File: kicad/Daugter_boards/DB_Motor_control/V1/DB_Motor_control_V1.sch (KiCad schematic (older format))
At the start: 11 parts, among them P1 CONN_01X19, P2 CONN_01X05, P3 CONN_01X03, P4 CONN_01X19, Q1 Q2N2222

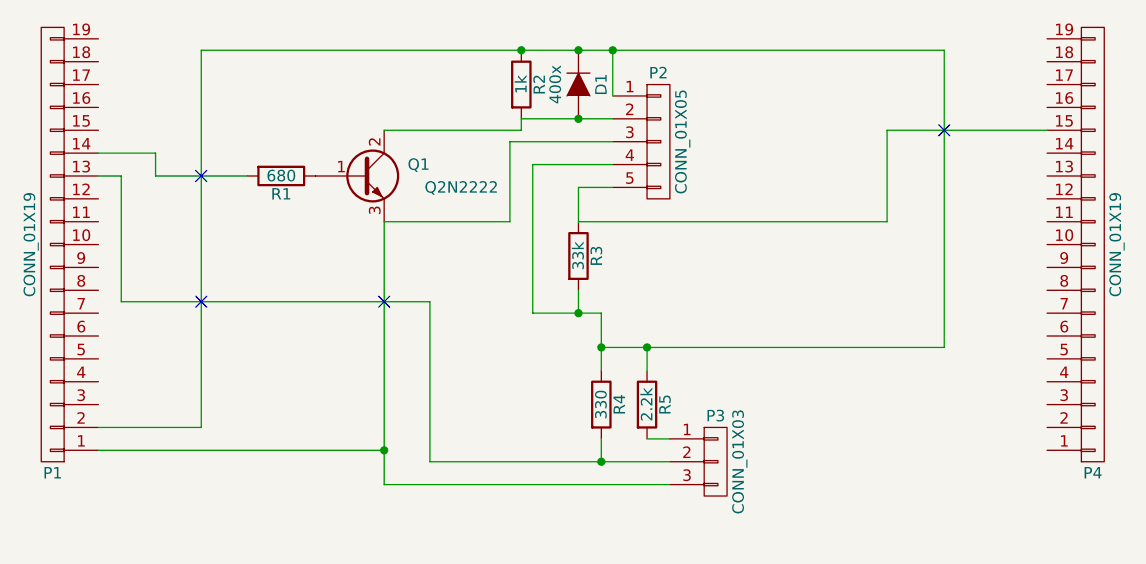
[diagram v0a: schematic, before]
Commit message: adding DB_Motor_Control
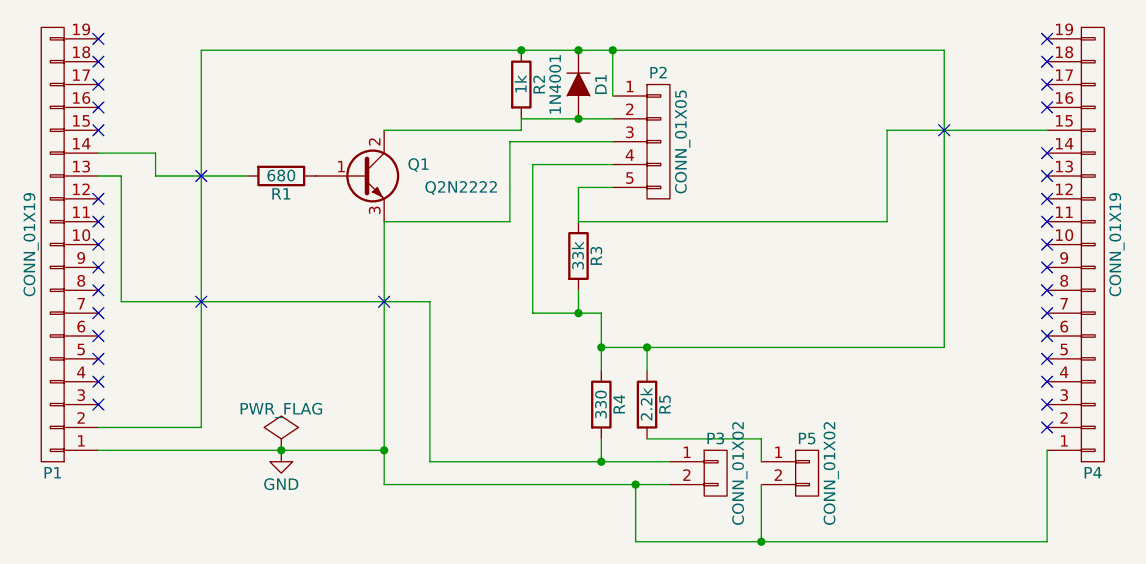
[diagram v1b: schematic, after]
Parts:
- removed P3: CONN_01X03, symbol CONN_01X03
- added P3, P5: CONN_01X02, Socket_Strips:Socket_Strip_Straight_1x02, symbol CONN_01X02
- D1: value 400x -> 1N4001; footprint (none) -> Diodes_ThroughHole:Diode_DO-35_SOD27_Horizontal_RM10
- P1, P4: footprint (none) -> Socket_Strips:Socket_Strip_Straight_1x19
- P2: footprint (none) -> Socket_Strips:Socket_Strip_Straight_1x05
- Q1: footprint (none) -> TO_SOT_Packages_THT:TO-18_3Pin
- R1, R2, R3, R4, R5: footprint (none) -> Resistors_ThroughHole:Resistor_Horizontal_RM10mm
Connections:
- net GND: now reaches P1.1 (P1), P2.3 (P3), Q1.3 (E)
- net GND: now also P4.1 (P1), P3.2 (P2), P5.2 (P2)
- net at R5.2: now also P5.1 (P1)
- net at P1.13 (P13), R4.2: now also P3.1 (P1)
- no-connect marks 4 -> 36
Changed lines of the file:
@@
 LIBS:valves
 LIBS:echopen
+LIBS:DB_Motor_control_V1-cache
 EELAYER 25 0
 EELAYER END
@@
 F 0 "R2" V 5280 2150 50  0000 C CNN
 F 1 "1k" V 5200 2150 50  0000 C CNN
-F 2 "" V 5130 2150 50  0000 C CNN
+F 2 "Resistors_ThroughHole:Resistor_Horizontal_RM10mm" V 5130 2150 50  0001 C CNN
 F 3 "" H 5200 2150 50  0000 C CNN
 	1    5200 2150
@@
 P 5450 2150
 F 0 "D1" H 5450 2250 50  0000 C CNN
-F 1 "400x" H 5450 2050 50  0000 C CNN
-F 2 "" H 5450 2150 50  0000 C CNN
+F 1 "1N4001" H 5450 2050 50  0000 C CNN
+F 2 "Diodes_ThroughHole:Diode_DO-35_SOD27_Horizontal_RM10" H 5450 2150 50  0001 C CNN
 F 3 "" H 5450 2150 50  0000 C CNN
 	1    5450 2150
@@
 F 0 "Q1" H 4800 2600 50  0000 R CNN
 F 1 "Q2N2222" H 5100 2500 50  0000 R CNN
-F 2 "" H 4700 2650 50  0000 C CNN
+F 2 "TO_SOT_Packages_THT:TO-18_3Pin" H 4700 2650 50  0001 C CNN
 F 3 "" H 4500 2550 50  0000 C CNN
 	1    4500 2550
@@
 F 0 "R1" V 4230 2550 50  0000 C CNN
 F 1 "680" V 4150 2550 50  0000 C CNN
-F 2 "" V 4080 2550 50  0000 C CNN
+F 2 "Resistors_ThroughHole:Resistor_Horizontal_RM10mm" V 4080 2550 50  0001 C CNN
 F 3 "" H 4150 2550 50  0000 C CNN
 	1    4150 2550
@@
 F 0 "R5" V 5830 3550 50  0000 C CNN
 F 1 "2.2k" V 5750 3550 50  0000 C CNN
-F 2 "" V 5680 3550 50  0000 C CNN
+F 2 "Resistors_ThroughHole:Resistor_Horizontal_RM10mm" V 5680 3550 50  0001 C CNN
 F 3 "" H 5750 3550 50  0000 C CNN
 	1    5750 3550
@@
 F 0 "R4" V 5630 3550 50  0000 C CNN
 F 1 "330" V 5550 3550 50  0000 C CNN
-F 2 "" V 5480 3550 50  0000 C CNN
+F 2 "Resistors_ThroughHole:Resistor_Horizontal_RM10mm" V 5480 3550 50  0001 C CNN
 F 3 "" H 5550 3550 50  0000 C CNN
 	1    5550 3550
@@
 Connection ~ 5600 2000
 Wire Wire Line
-	5850 3700 5750 3700
+	5750 3700 6250 3700
 Wire Wire Line
 	4800 3800 5850 3800
@@
 F 0 "R3" V 5530 2900 50  0000 C CNN
 F 1 "33k" V 5450 2900 50  0000 C CNN
-F 2 "" V 5380 2900 50  0000 C CNN
+F 2 "Resistors_ThroughHole:Resistor_Horizontal_RM10mm" V 5380 2900 50  0001 C CNN
 F 3 "" H 5450 2900 50  0000 C CNN
 	1    5450 2900
@@
 F 0 "P2" H 5800 2700 50  0000 C CNN
 F 1 "CONN_01X05" V 5900 2400 50  0000 C CNN
-F 2 "" H 5800 2400 50  0000 C CNN
+F 2 "Socket_Strips:Socket_Strip_Straight_1x05" H 5800 2400 50  0001 C CNN
 F 3 "" H 5800 2400 50  0000 C CNN
 	1    5800 2400
-	1    0    0    -1
-$EndComp
-$Comp
-L CONN_01X03 P3
-U 1 1 57A88844
-P 6050 3800
-F 0 "P3" H 6050 4000 50  0000 C CNN
-F 1 "CONN_01X03" V 6150 3800 50  0000 C CNN
-F 2 "" H 6050 3800 50  0000 C CNN
-F 3 "" H 6050 3800 50  0000 C CNN
-	1    6050 3800
 	1    0    0    -1
 $EndComp
@@
 F 0 "P1" H 3150 3850 50  0000 C CNN
 F 1 "CONN_01X19" V 3250 2850 50  0000 C CNN
-F 2 "" H 3150 2850 50  0000 C CNN
+F 2 "Socket_Strips:Socket_Strip_Straight_1x19" H 3150 2850 50  0001 C CNN
 F 3 "" H 3150 2850 50  0000 C CNN
 	1    3150 2850
@@
 F 0 "P4" H 7700 3850 50  0000 C CNN
 F 1 "CONN_01X19" V 7800 2850 50  0000 C CNN
-F 2 "" H 7700 2850 50  0000 C CNN
+F 2 "Socket_Strips:Socket_Strip_Straight_1x19" H 7700 2850 50  0001 C CNN
 F 3 "" H 7700 2850 50  0000 C CNN
 	1    7700 2850
@@
 NoConn ~ 4600 3100
 NoConn ~ 3800 3100
+$Comp
+L CONN_01X02 P3
+U 1 1 57B30B75
+P 6050 3850
+F 0 "P3" H 6050 4000 50  0000 C CNN
+F 1 "CONN_01X02" V 6150 3850 50  0000 C CNN
+F 2 "Socket_Strips:Socket_Strip_Straight_1x02" H 6050 3850 50  0001 C CNN
+F 3 "" H 6050 3850 50  0000 C CNN
+	1    6050 3850
+	1    0    0    -1
+$EndComp
+$Comp
+L CONN_01X02 P5
+U 1 1 57B30BB9
+P 6450 3850
+F 0 "P5" H 6450 4000 50  0000 C CNN
+F 1 "CONN_01X02" V 6550 3850 50  0000 C CNN
+F 2 "Socket_Strips:Socket_Strip_Straight_1x02" H 6450 3850 50  0001 C CNN
+F 3 "" H 6450 3850 50  0000 C CNN
+	1    6450 3850
+	1    0    0    -1
+$EndComp
+Wire Wire Line
+	6250 3700 6250 3800
+Wire Wire Line
+	5700 3900 5700 4150
+Wire Wire Line
+	5700 4150 7500 4150
+Wire Wire Line
+	6250 4150 6250 3900
+Connection ~ 5700 3900
+Wire Wire Line
+	7500 4150 7500 3750
+Connection ~ 6250 4150
+$Comp
+L PWR_FLAG #FLG01
+U 1 1 57B30CBF
+P 4150 3750
+F 0 "#FLG01" H 4150 3845 50  0001 C CNN
+F 1 "PWR_FLAG" H 4150 3930 50  0000 C CNN
+F 2 "" H 4150 3750 50  0000 C CNN
+F 3 "" H 4150 3750 50  0000 C CNN
+	1    4150 3750
+	1    0    0    -1
+$EndComp
+$Comp
+L GND #PWR02
+U 1 1 57B30CF7
+P 4150 3750
+F 0 "#PWR02" H 4150 3500 50  0001 C CNN
+F 1 "GND" H 4150 3600 50  0000 C CNN
+F 2 "" H 4150 3750 50  0000 C CNN
+F 3 "" H 4150 3750 50  0000 C CNN
+	1    4150 3750
+	1    0    0    -1
+$EndComp
+Connection ~ 4150 3750
+NoConn ~ 3350 1950
+NoConn ~ 3350 2050
+NoConn ~ 3350 2150
+NoConn ~ 3350 2250
+NoConn ~ 3350 2350
+NoConn ~ 3350 2750
+NoConn ~ 3350 2650
+NoConn ~ 3350 2850
+NoConn ~ 3350 2950
+NoConn ~ 3350 3050
+NoConn ~ 3350 3150
+NoConn ~ 3350 3250
+NoConn ~ 3350 3350
+NoConn ~ 3350 3450
+NoConn ~ 3350 3550
+NoConn ~ 7500 3650
+NoConn ~ 7500 3550
+NoConn ~ 7500 3450
+NoConn ~ 7500 3350
+NoConn ~ 7500 3250
+NoConn ~ 7500 3150
+NoConn ~ 7500 3050
+NoConn ~ 7500 2950
+NoConn ~ 7500 2850
+NoConn ~ 7500 2750
+NoConn ~ 7500 2650
+NoConn ~ 7500 2550
+NoConn ~ 7500 2450
+NoConn ~ 7500 2250
+NoConn ~ 7500 2150
+NoConn ~ 7500 2050
+NoConn ~ 7500 1950
 $EndSCHEMATC
